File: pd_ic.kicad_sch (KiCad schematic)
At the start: 7 parts, among them J11 Conn_01x02, Q1 IRF9540N, U13 CYPD3175-24LQXQ

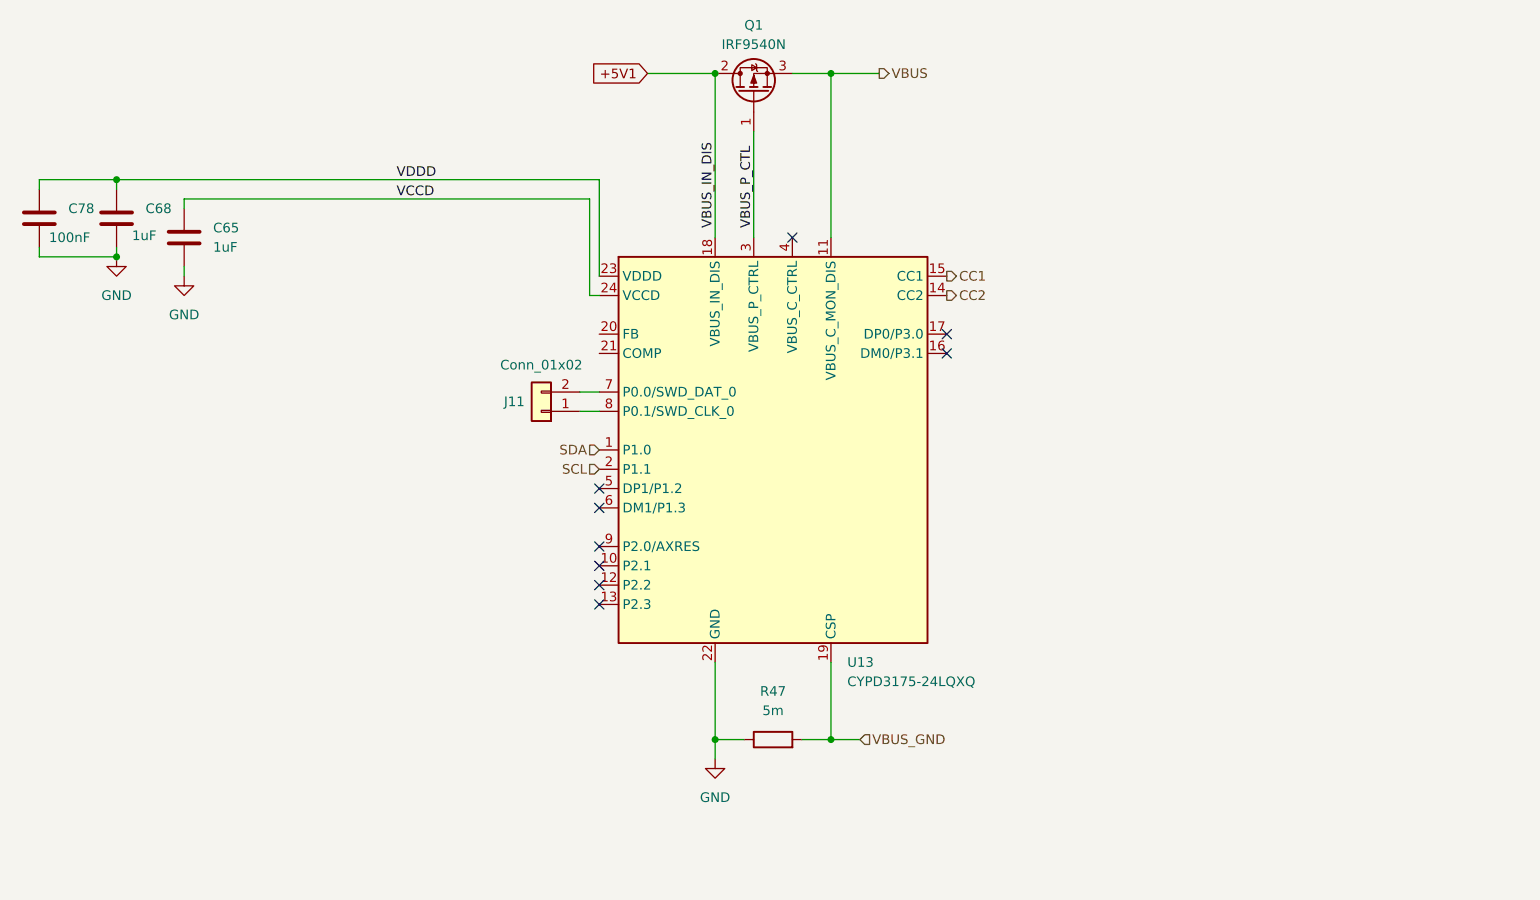
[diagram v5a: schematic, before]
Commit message: fixed usb c pd ic schematic
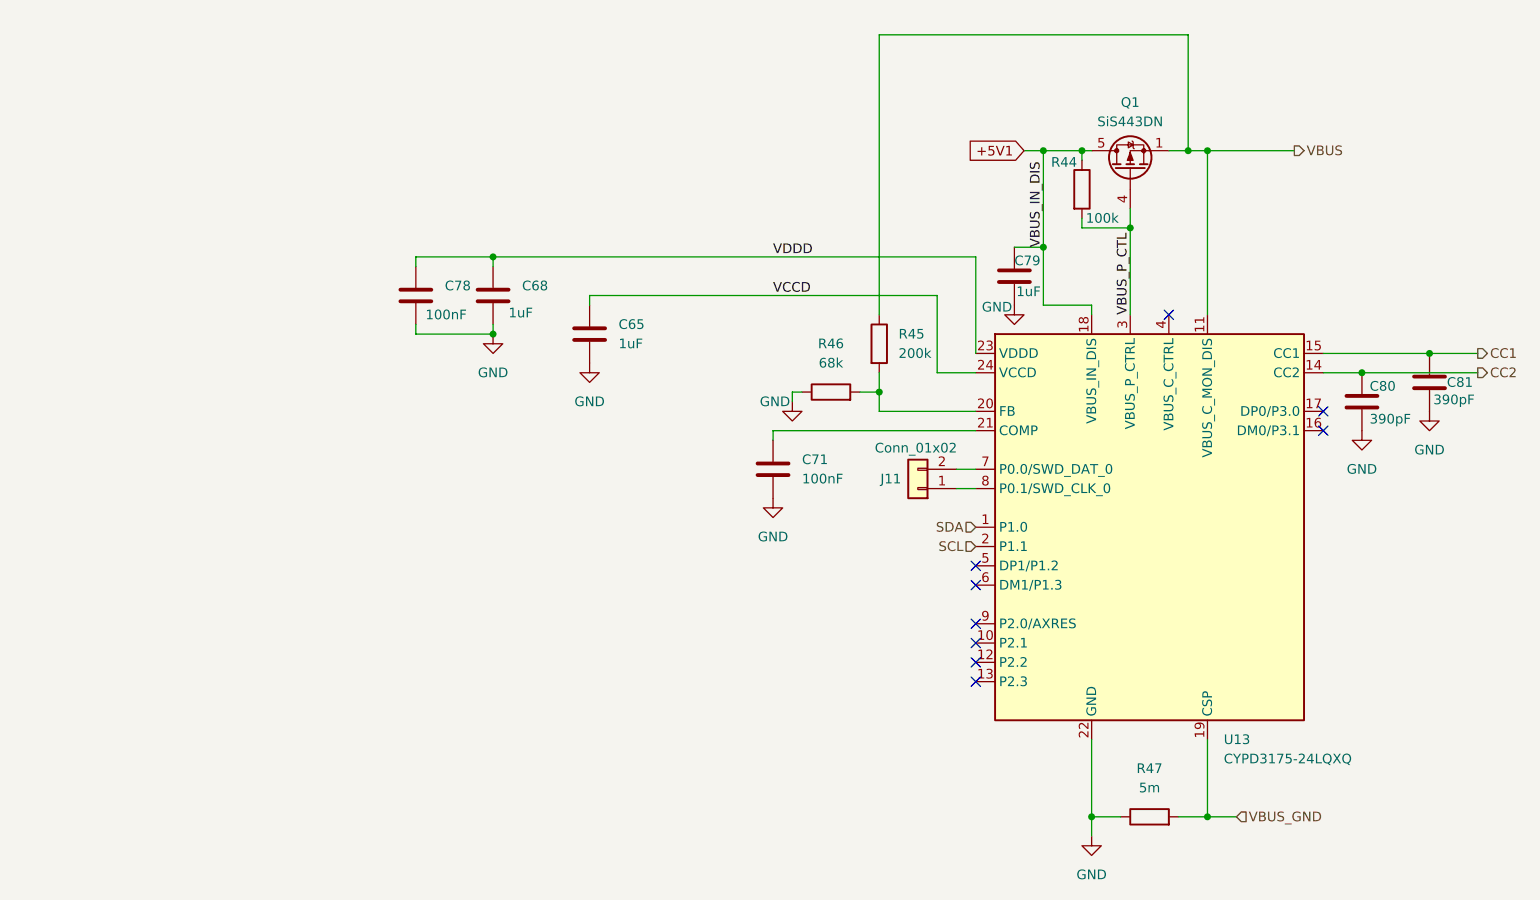
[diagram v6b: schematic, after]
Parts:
- removed Q1: IRF9540N, Package_TO_SOT_THT:TO-220-3_Horizontal_TabDown, symbol Transistor_FET:IRF9540N
- added C71: 100nF, symbol Device:C
- added C79: 1uF, symbol Device:C
- added C80, C81: 390pF, symbol Device:C
- added Q1: SiS443DN, Package_SO:Vishay_PowerPAK_1212-8_Single, symbol Transistor_FET:SiS443DN
- added R44: 100k, symbol Device:R
- added R45: 200k, symbol Device:R
- added R46: 68k, symbol Device:R
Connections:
- net +5V1: now also C79.1, Q1.5 (D), R44.1
- net CC1: now also C81.1
- net CC2: now also C80.1
- net GND: now also C71.2, C79.2, C80.2, C81.2, R46.1
- net VBUS: now also Q1.1 (S), Q1.2 (S), Q1.3 (S), R45.1
- net VBUS_P_CTL: now also Q1.4 (G), R44.2
- net at U13.20 (FB): now also R45.2, R46.2
- net at U13.21 (COMP): now also C71.1
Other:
- moved on the sheet: C65, C68, C78, J11, R47, U13

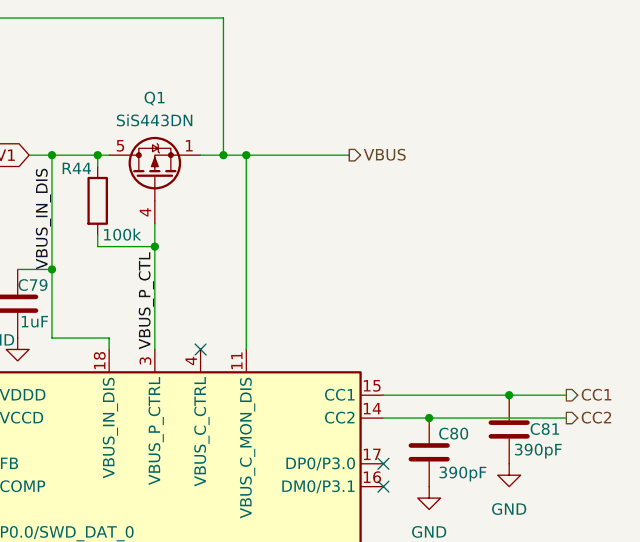
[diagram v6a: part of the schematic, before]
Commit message: added tvs diode to schematic of usb c port
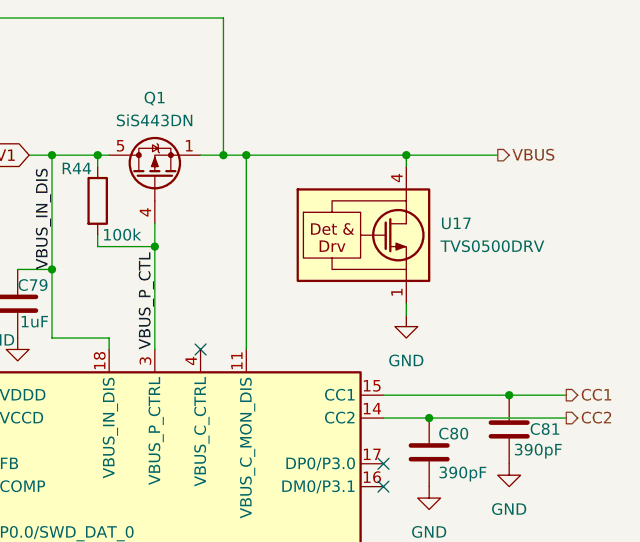
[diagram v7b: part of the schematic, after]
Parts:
- added U17: TVS0500DRV, Package_SON:WSON-6-1EP_2x2mm_P0.65mm_EP1x1.6mm, symbol Power_Protection:TVS0500DRV
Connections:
- net GND: now also U17.1 (GND), U17.2 (GND), U17.3 (GND), U17.7 (GND)
- net VBUS: now also U17.4 (IN), U17.5 (IN), U17.6 (IN)
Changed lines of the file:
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@@
+	)
+	(junction
+		(at 186.69 54.61)
+		(diameter 0)
+		(color 0 0 0 0)
 	)
 	(junction
@@
 	(wire
 		(pts
+			(xy 186.69 71.12) (xy 186.69 72.39)
+		)
+		(stroke
+			(width 0)
+			(type default)
+		)
+	)
+	(wire
+		(pts
 			(xy 147.32 67.31) (xy 147.32 74.93)
 		)
@@
 	(wire
 		(pts
+			(xy 186.69 54.61) (xy 196.85 54.61)
+		)
+		(stroke
+			(width 0)
+			(type default)
+		)
+	)
+	(wire
+		(pts
 			(xy 143.51 67.31) (xy 147.32 67.31)
 		)
@@
 	(wire
 		(pts
+			(xy 186.69 54.61) (xy 186.69 55.88)
+		)
+		(stroke
+			(width 0)
+			(type default)
+		)
+	)
+	(wire
+		(pts
 			(xy 147.32 54.61) (xy 152.4 54.61)
 		)
@@
 	(wire
 		(pts
-			(xy 168.91 54.61) (xy 180.34 54.61)
+			(xy 168.91 54.61) (xy 186.69 54.61)
 		)
 		(stroke
@@
 	(hierarchical_label "VBUS"
 		(shape output)
-		(at 180.34 54.61 0)
+		(at 196.85 54.61 0)
 		(effects
 			(font
@@
 					(unit 1)
 				)
+			)
+		)
+	)
+	(symbol
+		(lib_id "power:GND")
+		(at 186.69 72.39 0)
+		(unit 1)
+		(exclude_from_sim no)
+		(in_bom yes)
+		(on_board yes)
+		(dnp no)
+		(fields_autoplaced yes)
+		(property "Reference" "#PWR068"
+			(at 186.69 78.74 0)
+			(effects
+				(font
+					(size 1.27 1.27)
+				)
+				(hide yes)
+			)
+		)
+		(property "Value" "GND"
+			(at 186.69 77.47 0)
+			(effects
+				(font
+					(size 1.27 1.27)
+				)
+			)
+		)
+		(property "Footprint" ""
+			(at 186.69 72.39 0)
+			(effects
+				(font
+					(size 1.27 1.27)
+				)
+				(hide yes)
+			)
+		)
+		(property "Datasheet" ""
+			(at 186.69 72.39 0)
+			(effects
+				(font
+					(size 1.27 1.27)
+				)
+				(hide yes)
+			)
+		)
+		(property "Description" "Power symbol creates a global label with name \"GND\" , ground"
+			(at 186.69 72.39 0)
+			(effects
+				(font
+					(size 1.27 1.27)
+				)
+				(hide yes)
+			)
+		)
+		(pin "1"
+		)
+		(instances
+			(project ""
+				(path "/2f56b371-1597-47e1-a48d-b7f69d342f77/a0987cd4-dfa7-4cf4-a9f1-5b392786bba7"
+					(reference "#PWR068")
+					(unit 1)
+				)
+			)
+		)
+	)
+	(symbol
+		(lib_id "Power_Protection:TVS0500DRV")
+		(at 186.69 63.5 0)
+		(unit 1)
+		(exclude_from_sim no)
+		(in_bom yes)
+		(on_board yes)
+		(dnp no)
+		(fields_autoplaced yes)
+		(property "Reference" "U17"
+			(at 190.5 62.2299 0)
+			(effects
+				(font
+					(size 1.27 1.27)
+				)
+				(justify left)
+			)
+		)
+		(property "Value" "TVS0500DRV"
+			(at 190.5 64.7699 0)
+			(effects
+				(font
+					(size 1.27 1.27)
+				)
+				(justify left)
+			)
+		)
+		(property "Footprint" "Package_SON:WSON-6-1EP_2x2mm_P0.65mm_EP1x1.6mm"
+			(at 191.77 72.39 0)
+			(effects
+				(font
+					(size 1.27 1.27)
+				)
+				(hide yes)
+			)
+		)
+		(property "Datasheet" "http://www.ti.com/lit/ds/symlink/tvs0500.pdf"
+			(at 184.15 63.5 0)
+			(effects
+				(font
+					(size 1.27 1.27)
+				)
+				(hide yes)
+			)
+		)
+		(property "Description" "Flat-Clamp Surge Protection Device. 5Vrwm, WSON-6"
+			(at 186.69 63.5 0)
+			(effects
+				(font
+					(size 1.27 1.27)
+				)
+				(hide yes)
+			)
+		)
+		(pin "6"
+		)
+		(pin "5"
+		)
+		(pin "1"
+		)
+		(pin "7"
+		)
+		(pin "3"
+		)
+		(pin "2"
+		)
+		(pin "4"
+		)
+		(instances
+			(project ""
+				(path "/2f56b371-1597-47e1-a48d-b7f69d342f77/a0987cd4-dfa7-4cf4-a9f1-5b392786bba7"
+					(reference "U17")
+					(unit 1)
+				)

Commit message: added new stuff to pcb
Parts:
- C71, C79, C80, C81: footprint (none) -> Capacitor_SMD:C_0402_1005Metric
- R44, R45, R46: footprint (none) -> Resistor_SMD:R_0402_1005Metric
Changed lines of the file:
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@@
 			)
 		)
-		(property "Footprint" ""
+		(property "Footprint" "Capacitor_SMD:C_0402_1005Metric"
 			(at 112.7252 100.33 0)
 			(effects
@@
 			)
 		)
-		(property "Footprint" ""
+		(property "Footprint" "Resistor_SMD:R_0402_1005Metric"
 			(at 119.38 88.138 90)
 			(effects
@@
 			)
 		)
-		(property "Footprint" ""
+		(property "Footprint" "Resistor_SMD:R_0402_1005Metric"
 			(at 123.952 80.01 90)
 			(effects
@@
 			)
 		)
-		(property "Footprint" ""
+		(property "Footprint" "Capacitor_SMD:C_0402_1005Metric"
 			(at 199.0852 88.9 0)
 			(effects
@@
 			)
 		)
-		(property "Footprint" ""
+		(property "Footprint" "Resistor_SMD:R_0402_1005Metric"
 			(at 150.622 59.69 90)
 			(effects
@@
 			)
 		)
-		(property "Footprint" ""
+		(property "Footprint" "Capacitor_SMD:C_0402_1005Metric"
 			(at 190.1952 91.44 0)
 			(effects
@@
 			)
 		)
-		(property "Footprint" ""
+		(property "Footprint" "Capacitor_SMD:C_0402_1005Metric"
 			(at 144.4752 74.93 0)
 			(effects
